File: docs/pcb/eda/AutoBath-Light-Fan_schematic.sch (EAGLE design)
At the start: 44 parts, among them K1 5V SPDT (light), K2 5V SPDT (fan), Q1 S8050, Q2 S8050, U1 GD32F103C8T6

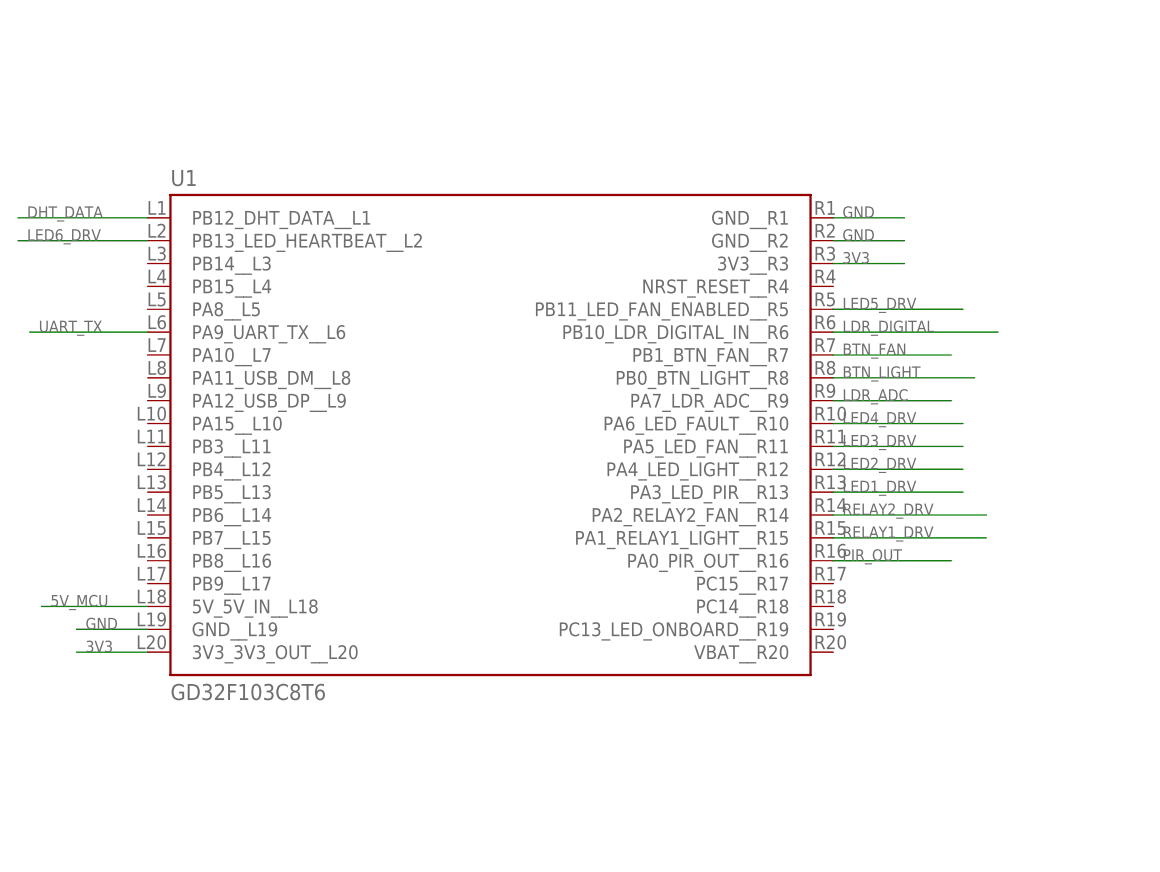
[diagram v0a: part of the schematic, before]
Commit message: Blue Pill symbol with numbered pins 1-40 and plain names, pinout picture
Co-Authored-By: manoranjan2050 <manoranjan2050@live.com>
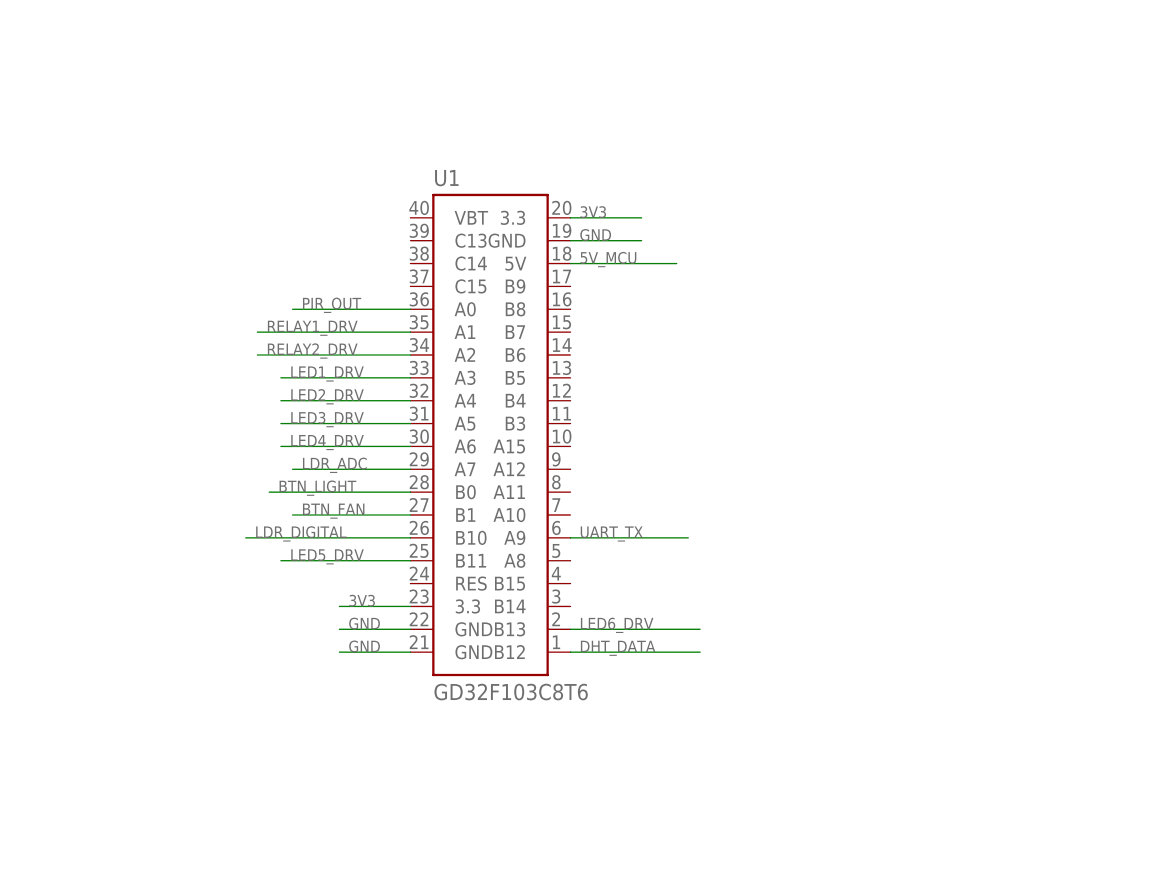
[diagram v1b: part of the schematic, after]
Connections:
- net 3V3: now also U1.3.3, U1.3.3​; no longer U1.3V3_3V3_OUT__L20, U1.3V3__R3
- net 5V_MCU: now also U1.5V; no longer U1.5V_5V_IN__L18
- net BTN_FAN: now also U1.B1; no longer U1.PB1_BTN_FAN__R7
- net BTN_LIGHT: now also U1.B0; no longer U1.PB0_BTN_LIGHT__R8
- net DHT_DATA: now also U1.B12; no longer U1.PB12_DHT_DATA__L1
- net GND: now also U1.GND, U1.GND​, U1.GND​​; no longer U1.GND__L19, U1.GND__R1, U1.GND__R2
- net LDR_ADC: now also U1.A7; no longer U1.PA7_LDR_ADC__R9
- net LDR_DIGITAL: now also U1.B10; no longer U1.PB10_LDR_DIGITAL_IN__R6
- net LED1_DRV: now also U1.A3; no longer U1.PA3_LED_PIR__R13
- net LED2_DRV: now also U1.A4; no longer U1.PA4_LED_LIGHT__R12
- net LED3_DRV: now also U1.A5; no longer U1.PA5_LED_FAN__R11
- net LED4_DRV: now also U1.A6; no longer U1.PA6_LED_FAULT__R10
- net LED5_DRV: now also U1.B11; no longer U1.PB11_LED_FAN_ENABLED__R5
- net LED6_DRV: now also U1.B13; no longer U1.PB13_LED_HEARTBEAT__L2
- net PIR_OUT: now also U1.A0; no longer U1.PA0_PIR_OUT__R16
- net RELAY1_DRV: now also U1.A1; no longer U1.PA1_RELAY1_LIGHT__R15
- net RELAY2_DRV: now also U1.A2; no longer U1.PA2_RELAY2_FAN__R14
- net UART_TX: now also U1.A9; no longer U1.PA9_UART_TX__L6
